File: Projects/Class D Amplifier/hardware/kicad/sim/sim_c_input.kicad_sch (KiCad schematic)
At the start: 10 parts, among them U1 TL074, U2 TL074

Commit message: Class D amp: link the testbenches from the board sheet, both ways
The board schematic now carries a SIMULATION index in the free space below the
bridge: one clickable line per testbench, opening that testbench's project.
Each testbench carries a link back to the board.

These are hyperlinks, not hierarchical sheets, and that was not the first
choice - it is the result of trying the obvious thing and measuring what it
did. Attaching sim_b_triangle to classd.kicad_sch as a hierarchical sheet and
exporting the netlist showed three separate kinds of damage: the testbench's
12 V source welded straight onto the board's +12V rail, taking it from 23 pins
to 25; the sim's sources landing in the board netlist ready for Update PCB
from Schematic to push them onto copper; and worst, the sim sheet's U1, R4 and
R5 silently merging with the board parts of the same name, quietly rewiring
real components. A hierarchy is one electrical design, so anything inside it
is part of the board whether you meant it or not.

Getting the hyperlink right took measuring too. KiCad 10 refuses to load a
schematic where the link is spelled (hyperlink ...) as it is on the PCB, or
where it sits beside (uuid ...) rather than inside (effects ...). It also
rejects an href that is a bare relative path or a ${KIPRJMOD} variable, but
accepts a relative path carrying the file: scheme - which is what is used, so
the links survive the repository being checked out anywhere.

Also fixed while here: labels that sat beside a wire end rather than on it
left dangling endpoints, and the testbench supplies needed a ground PWR_FLAG
as well as a rail one. All four sheets now pass ERC with zero violations, and
the simulation checks still pass 16/16.
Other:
- note added: "<- back to the board schematic classd.kicad_pro"
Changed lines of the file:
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@@
+	(wire
+		(pts
+			(xy 17.78 38.1) (xy 27.94 38.1)
+		)
+		(stroke
+			(width 0)
+			(type default)
+		)
+	)
 	(wire
 		(pts
@@
 	(junction
 		(at 17.78 27.94)
+		(diameter 0)
+		(color 0 0 0 0)
+	)
+	(junction
+		(at 17.78 38.1)
 		(diameter 0)
 		(color 0 0 0 0)
@@
 	)
 	(label "AUDIO_N"
-		(at 167.64 58.42 0)
+		(at 172.72 58.42 0)
 		(effects
 			(font
@@
 		)
 	)
+	(text "<-  back to the board schematic   classd.kicad_pro"
+		(at 12.7 111.76 0)
+		(effects
+			(font
+				(size 1.6 1.6)
+			)
+			(justify left bottom)
+			(href "file:../classd.kicad_pro")
+		)
+	)
 	(symbol
 		(lib_id "Simulation_SPICE:VDC")
@@
 	)
 	(symbol
+		(lib_id "power:PWR_FLAG")
+		(at 27.94 38.1 0)
+		(unit 1)
+		(body_style 1)
+		(exclude_from_sim no)
+		(in_bom no)
+		(on_board no)
+		(in_pos_files no)
+		(dnp no)
+		(property "Reference" "#PWR004"
+			(at 30.734 36.83 0)
+			(hide yes)
+			(show_name no)
+			(do_not_autoplace no)
+			(effects
+				(font
+					(size 1.27 1.27)
+				)
+			)
+		)
+		(property "Value" "PWR_FLAG"
+			(at 30.734 39.37 0)
+			(show_name no)
+			(do_not_autoplace no)
+			(effects
+				(font
+					(size 1.27 1.27)
+				)
+			)
+		)
+		(property "Footprint" ""
+			(at 27.94 38.1 0)
+			(hide yes)
+			(show_name no)
+			(do_not_autoplace no)
+			(effects
+				(font
+					(size 1.27 1.27)
+				)
+			)
+		)
+		(property "Datasheet" ""
+			(at 27.94 38.1 0)
+			(hide yes)
+			(show_name no)
+			(do_not_autoplace no)
+			(effects
+				(font
+					(size 1.27 1.27)
+				)
+			)
+		)
+		(instances
+			(project "sim_c_input"
+				(path "/a1000000-0000-4000-8000-000000000003"
+					(reference "#PWR004")
+					(unit 1)
+				)
+			)
+		)
+	)
+	(symbol
 		(lib_id "Simulation_SPICE:VDC")
 		(at 17.78 58.42 0)
@@
 		(in_pos_files no)
 		(dnp no)
-		(property "Reference" "#PWR004"
+		(property "Reference" "#PWR005"
 			(at 20.828 67.31 0)
 			(hide yes)
@@
 			(project "sim_c_input"
 				(path "/a1000000-0000-4000-8000-000000000003"
-					(reference "#PWR004")
+					(reference "#PWR005")
 					(unit 1)
 				)
@@
 		(in_pos_files no)
 		(dnp no)
-		(property "Reference" "#PWR005"
+		(property "Reference" "#PWR006"
 			(at 41.148 67.31 0)
 			(hide yes)
@@
 			(project "sim_c_input"
 				(path "/a1000000-0000-4000-8000-000000000003"
-					(reference "#PWR005")
+					(reference "#PWR006")
 					(unit 1)
 				)
@@
 		(in_pos_files no)
 		(dnp no)
-		(property "Reference" "#PWR006"
+		(property "Reference" "#PWR007"
 			(at 83.82 46.99 0)
 			(hide yes)
@@
 			(project "sim_c_input"
 				(path "/a1000000-0000-4000-8000-000000000003"
-					(reference "#PWR006")
+					(reference "#PWR007")
 					(unit 1)
 				)
@@
 		(in_pos_files no)
 		(dnp no)
-		(property "Reference" "#PWR007"
+		(property "Reference" "#PWR008"
 			(at 84.328 72.39 0)
 			(hide yes)
@@
 			(project "sim_c_input"
 				(path "/a1000000-0000-4000-8000-000000000003"
-					(reference "#PWR007")
+					(reference "#PWR008")
 					(unit 1)
 				)
@@
 		(in_pos_files no)
 		(dnp no)
-		(property "Reference" "#PWR008"
+		(property "Reference" "#PWR009"
 			(at 147.32 44.45 0)
 			(hide yes)
@@
 			(project "sim_c_input"
 				(path "/a1000000-0000-4000-8000-000000000003"
-					(reference "#PWR008")
+					(reference "#PWR009")
 					(unit 1)
 				)
@@
 		(in_pos_files no)
 		(dnp no)
-		(property "Reference" "#PWR009"
+		(property "Reference" "#PWR010"
 			(at 144.78 69.342 0)
 			(hide yes)
@@
 			(project "sim_c_input"
 				(path "/a1000000-0000-4000-8000-000000000003"
-					(reference "#PWR009")
-					(unit 1)
-				)
+					(reference "#PWR010")
+					(unit 1)
+				)

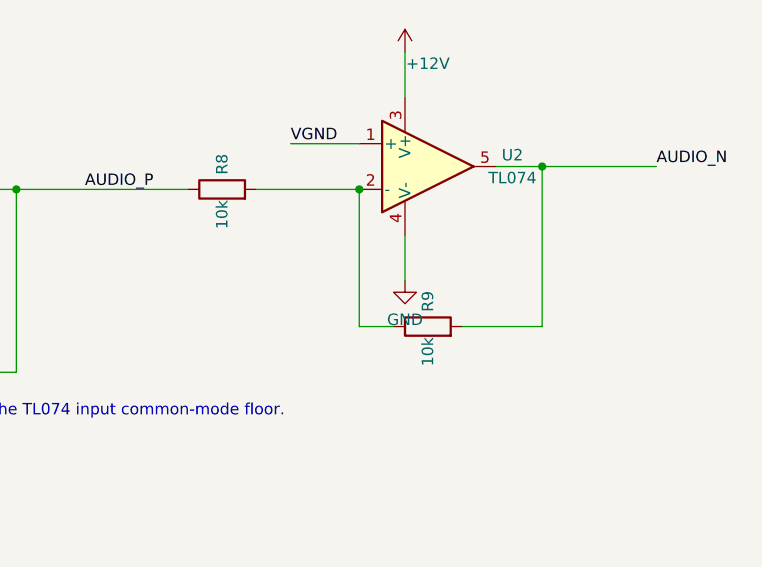
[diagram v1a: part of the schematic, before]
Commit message: Class D amp: the remaining three testbenches, E, F and G
E drives the CD4049 complement chain into the HIP4082 and measures what the
dead-time resistor actually buys: 225 ns with both gates off, never both on,
and a bootstrap that fills in ~50 us and settles one Schottky drop below the
rail. The switch nodes need holding down for that -- left floating they drift
up through the driver's own leakage until the bootstrap caps have barely a
volt across them, so R23/R24 stand in for the low-side FET being on.

F puts four real IRF540N cards, body diode included, under the driver and runs
them into the LC filter and a 4 ohm load at a fixed 79/21 duty: 11.75 W with
0.28 Vpp of carrier left on the output.

G is the whole chain, audio in to speaker out, and it is the one that answers
the design question. It makes 13 W -- and at that level AUDIO_P bottoms out at
4.00 V, which is the TL074's input common-mode floor. Full output and the
input stage's limit coincide exactly; there is no headroom to trade. That was
flagged on paper in the build notes and is now a number the harness asserts.

Three fixes fell out of building them, all in code that had never been
exercised because no bench used it before:

- the IRF540N Sim.Pins map said 1=D 2=G, but the symbol numbers its pins to
  the TO-220 pinout, 1=G 2=D. The bridge would have simulated as four
  transistors wired gate to drain.
- KiCad validates every Sim.Params key against the subcircuit's own parameter
  list and refuses the netlist export for one it cannot find, so the HIP4082's
  dead time moves from an internal .param to the .subckt line.
- a sym-lib-table registers the vendored CD4049 symbol, clearing the
  lib_symbol_issues ERC violations on every sheet that uses it.

The driver, bridge and filter are now drawn once and translated onto the three
sheets, with the geometry taken from the matching block of the board's own
layout script -- a bootstrap wired one way on the board and another way in its
testbench proves nothin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
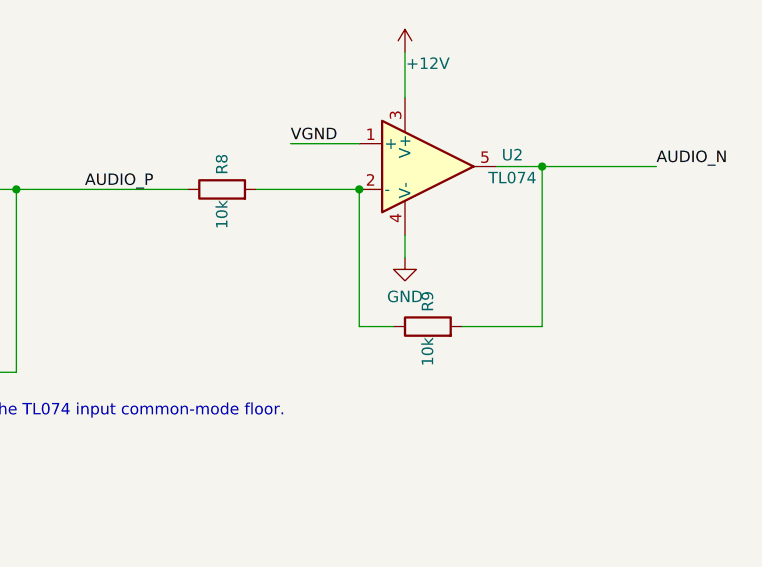
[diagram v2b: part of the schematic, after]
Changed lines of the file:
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@@
 	(wire
 		(pts
-			(xy 144.78 66.04) (xy 144.78 71.12)
+			(xy 144.78 66.04) (xy 144.78 68.58)
 		)
 		(stroke
@@
 	(symbol
 		(lib_id "power:GND")
-		(at 144.78 71.12 0)
+		(at 144.78 68.58 0)
 		(unit 1)
 		(body_style 1)
@@
 		(dnp no)
 		(property "Reference" "#PWR010"
-			(at 144.78 69.342 0)
+			(at 144.78 66.802 0)
 			(hide yes)
 			(show_name no)
@@
 		)
 		(property "Value" "GND"
-			(at 144.78 75.438 0)
-			(show_name no)
-			(do_not_autoplace no)
-			(effects
-				(font
-					(size 1.27 1.27)
-				)
-			)
-		)
-		(property "Footprint" ""
-			(at 144.78 71.12 0)
-			(hide yes)
-			(show_name no)
-			(do_not_autoplace no)
-			(effects
-				(font
-					(size 1.27 1.27)
-				)
-			)
-		)
-		(property "Datasheet" ""
-			(at 144.78 71.12 0)
-			(hide yes)
-			(show_name no)
+			(at 144.78 72.898 0)
+			(show_name no)
+			(do_not_autoplace no)
+			(effects
+				(font
+					(size 1.27 1.27)
+				)
+			)
+		)
+		(property "Footprint" ""
+			(at 144.78 68.58 0)
+			(hide yes)
+			(show_name no)
+			(do_not_autoplace no)
+			(effects
+				(font
+					(size 1.27 1.27)
+				)
+			)
+		)
+		(property "Datasheet" ""
+			(at 144.78 68.58 0)
+			(hide yes)
+			(show_name no)

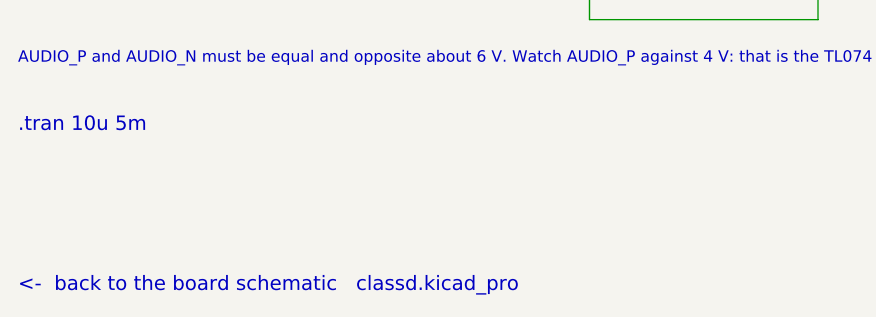
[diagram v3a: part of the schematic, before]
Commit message: Class D amp: point the simulation links at the sheets, not the projects
Clicking a link opened the project manager and left you one click short of
the drawing. Windows resolves the two extensions to different programs:

  .kicad_pro -> kicad.exe     the project manager
  .kicad_sch -> eeschema.exe  the schematic editor, straight onto the sheet

So the board's index and the benches' back-links now name the .kicad_sch.
Eeschema still picks up the matching .kicad_pro sitting beside it, which is
what carries the netclass and the simulator workbook, so nothing is lost by
skipping the project manager.

Note for anyone setting this up on another machine: the association has to
point at the KiCad version the files were written with. On this PC
.kicad_sch resolved to the 9.0 eeschema while .kicad_pro resolved to 10.0,
and a 9.0 editor cannot open a 10.0 schematic.
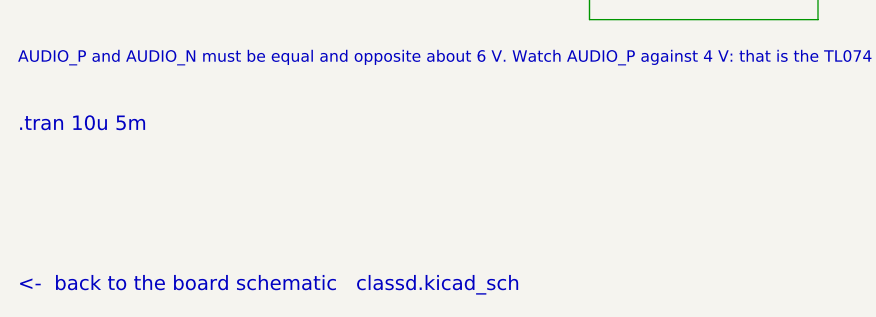
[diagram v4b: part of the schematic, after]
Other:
- note added: "<- back to the board schematic classd.kicad_sch"
- note removed: "<- back to the board schematic classd.kicad_pro"
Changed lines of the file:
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@@
 		)
 	)
-	(text "<-  back to the board schematic   classd.kicad_pro"
+	(text "<-  back to the board schematic   classd.kicad_sch"
 		(at 12.7 111.76 0)
 		(effects
@@
 			)
 			(justify left bottom)
-			(href "file:../classd.kicad_pro")
+			(href "file:../classd.kicad_sch")
 		)
 	)
